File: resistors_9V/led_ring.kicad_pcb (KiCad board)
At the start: 2 copper layers, 24.1 x 31.8 mm, 15 parts, among them J1 Conn_01x02, M1 MOUNT_HOLE_4-40, M2 MOUNT_HOLE_4-40

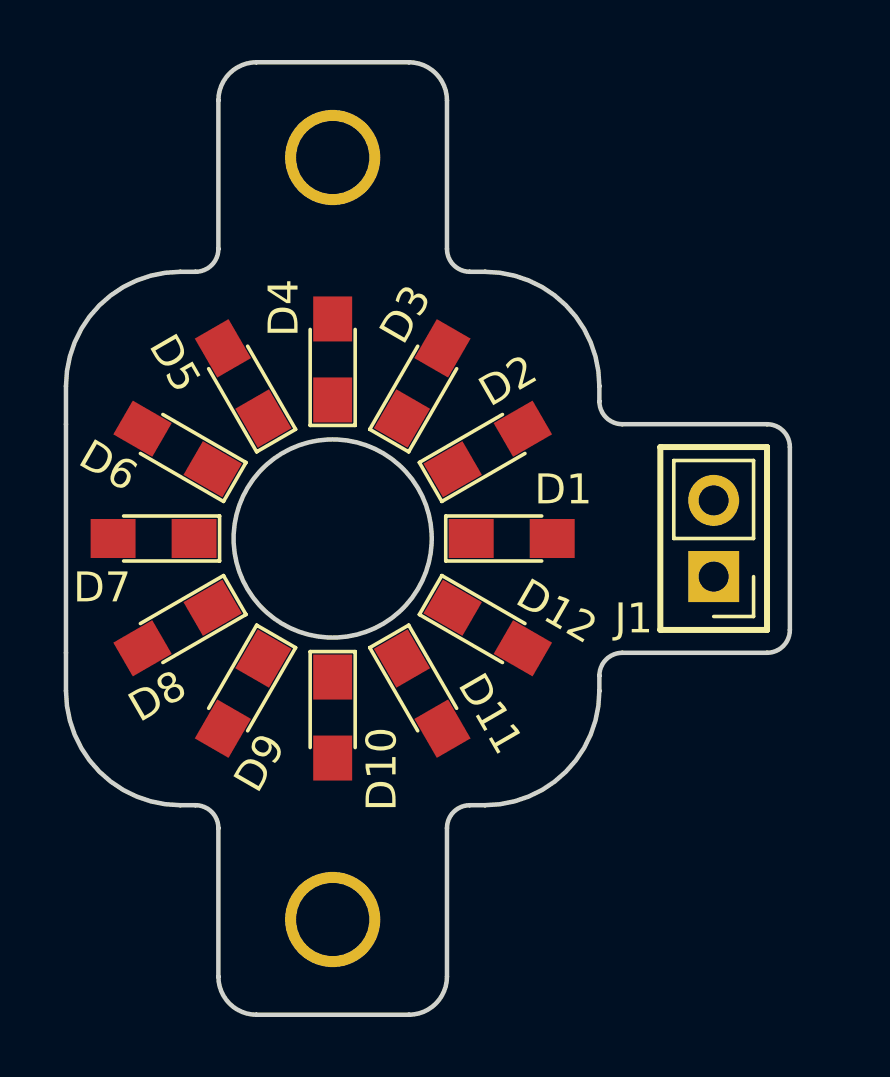
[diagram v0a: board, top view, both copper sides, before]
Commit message: Finished 9V design w/ current limiting resistors.
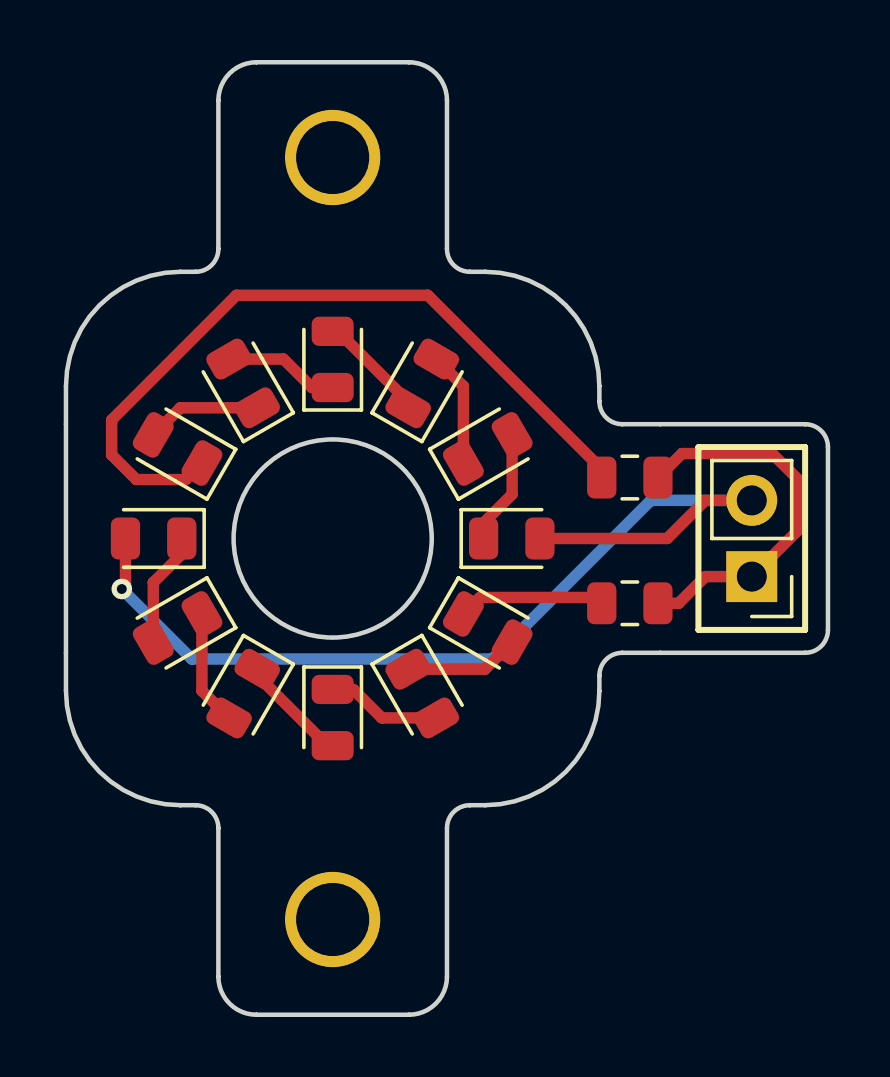
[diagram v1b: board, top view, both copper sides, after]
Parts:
- added R1: 75, Resistor_SMD:R_0805_2012Metric, F.Cu at (60.7, 53.0)
- added R2: 75, Resistor_SMD:R_0805_2012Metric, F.Cu at (60.7, 48.8)
- D1, D10, D11, D12, D2, D3, D4, D5, D6, D7, D8, D9: footprint LEDs:LED_0805_HandSoldering -> LED_SMD:LED_0805_2012Metric
- moved J1 1.27 mm to (64.8, 52.1)
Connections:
- D12 pad 1: GND -> Net-(D12-Pad1)
- D7 pad 2: Net-(D6-Pad1) -> Net-(D1-Pad2)
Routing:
- net Net-(D1-Pad2): track 0.00 -> 33.5 mm, vias 0 -> 1
- net Net-(D6-Pad1): track 0.00 -> 25.5 mm
- net GND: track 0.00 -> 12.7 mm
- net Net-(D12-Pad1): track 0.00 -> 4.92 mm
- net Net-(D7-Pad1): track 0.00 -> 3.85 mm
- net Net-(D10-Pad1): track 0.00 -> 3.85 mm
- net Net-(D4-Pad1): track 0.00 -> 3.85 mm
- net Net-(D1-Pad1): track 0.00 -> 3.85 mm
- net Net-(D8-Pad1): track 0.00 -> 3.84 mm
- net Net-(D11-Pad1): track 0.00 -> 3.84 mm
- net Net-(D5-Pad1): track 0.00 -> 3.84 mm
- net Net-(D2-Pad1): track 0.00 -> 3.84 mm
- net Net-(D3-Pad1): track 0.00 -> 3.69 mm
- net Net-(D10-Pad2): track 0.00 -> 3.69 mm
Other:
- board size 24.1 x 31.8 mm -> 25.4 x 31.8 mm
- net class Default: clearance 0.2032 -> 0.508
- rule trace_clearance: 0.2032 -> 0.508
- board text added: "9V"
- board text added: "9V IR LED Ring V0.1"
- board text added: "Dickinson Lab 2020"
- board text added: "GND"
- board text removed: "Dickinson Lab 2018"
- board text removed: "IR LED Ring V0.1"
